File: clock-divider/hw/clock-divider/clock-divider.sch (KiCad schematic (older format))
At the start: 15 parts

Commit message: clock-divider: schematic++
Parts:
- added C? (x2): 22p, symbol Device:C
- added D?: Beat, symbol Device:LED
- added J?: AVR-ISP-6, symbol Connector:AVR-ISP-6
- added J?: Trigger Next Seq, symbol Connector:AudioJack3
- added Q? (x2): BC548, Package_TO_SOT_THT:TO-92_Inline, symbol Transistor_BJT:BC548
- added R? (x3): 3.3k, symbol Device:R
- added R?: R, symbol Device:R
- added R? (x9): 150, symbol Device:R
- added R? (x2): 10k, symbol Device:R
- added RV?: VAL_IN, symbol Device:R_POT
- added RV?: VAL_OUT, symbol Device:R_POT
- added SW?: Mode_in, symbol Switch:SW_Push
- added SW?: Mode_out, symbol Switch:SW_Push
- added SW?: Disp_next_seq, symbol Switch:SW_Push
- added U?: Left, Display_7Segment:HDSP-7801, symbol Display_Character:HDSP-7803
- added U?: Right, Display_7Segment:HDSP-7801, symbol Display_Character:HDSP-7803
- added Y?: 10MHz, symbol Device:Crystal
- C? (x2): value CP -> 100µ
- D? (x3): value D -> 1N4148
- R?: value R -> 10k
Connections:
- net labels added: +5V, 7seg_a, 7seg_b, 7seg_c, 7seg_d, 7seg_dp, 7seg_e, 7seg_f, 7seg_g, 7seg_sel_left, 7seg_sel_right, act_in, act_out, disp_next_seq, miso, mosi, sck, trig_next_seq, value_in, value_out, ~reset
- wire segments 38 -> 86
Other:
- moved on the sheet: R?, U?

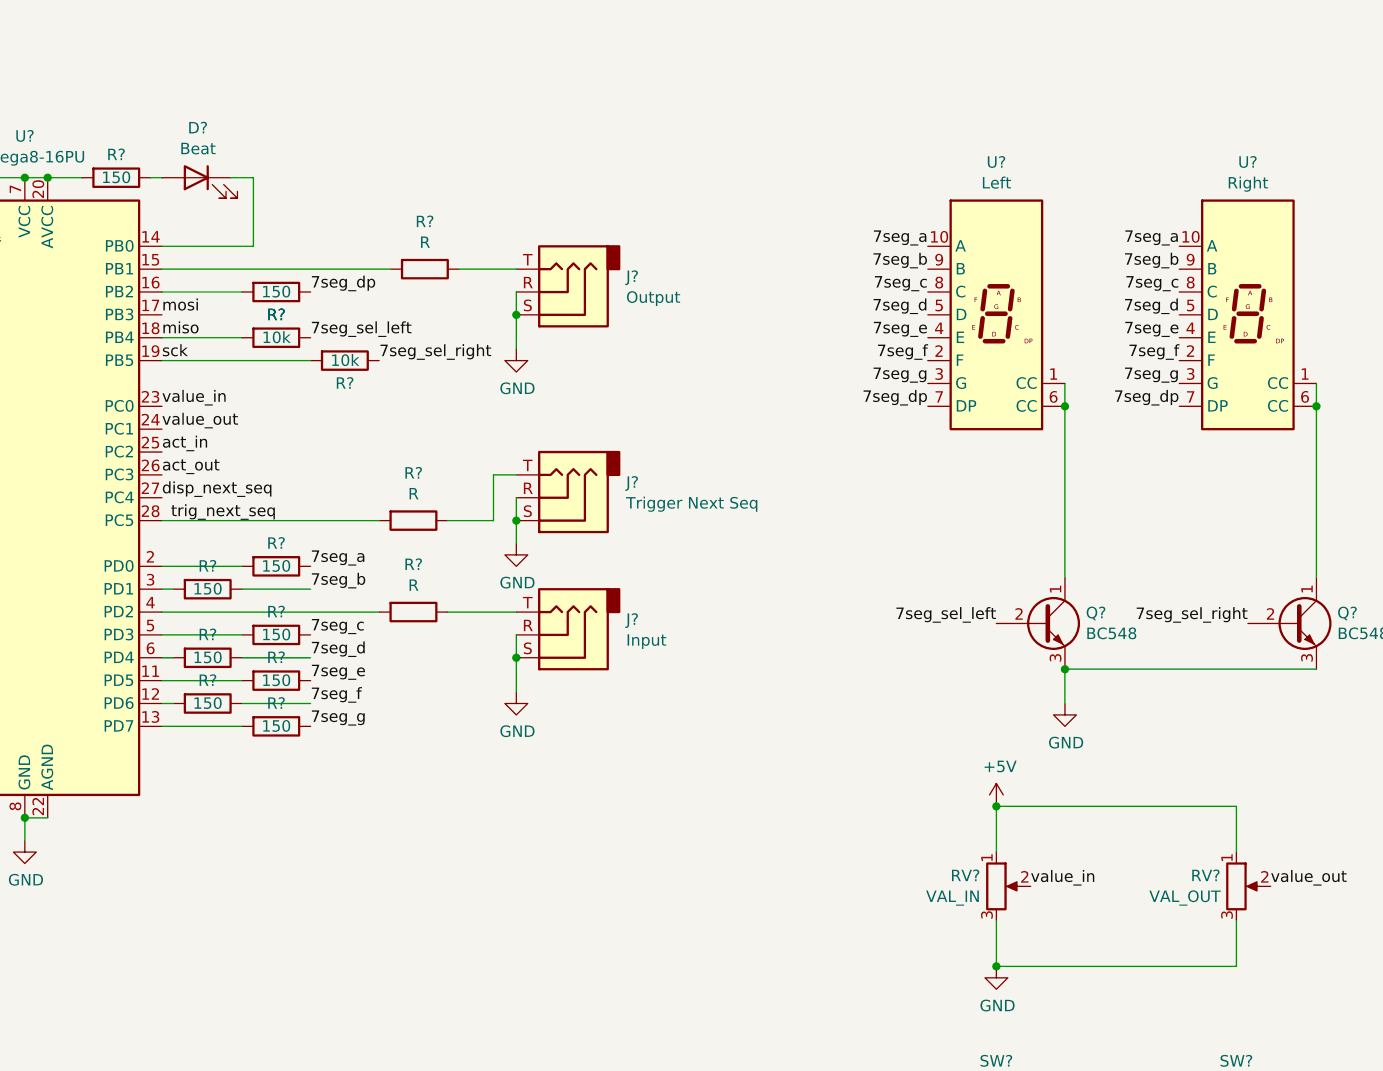
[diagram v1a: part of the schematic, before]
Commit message: clock-divider: add protection diodes
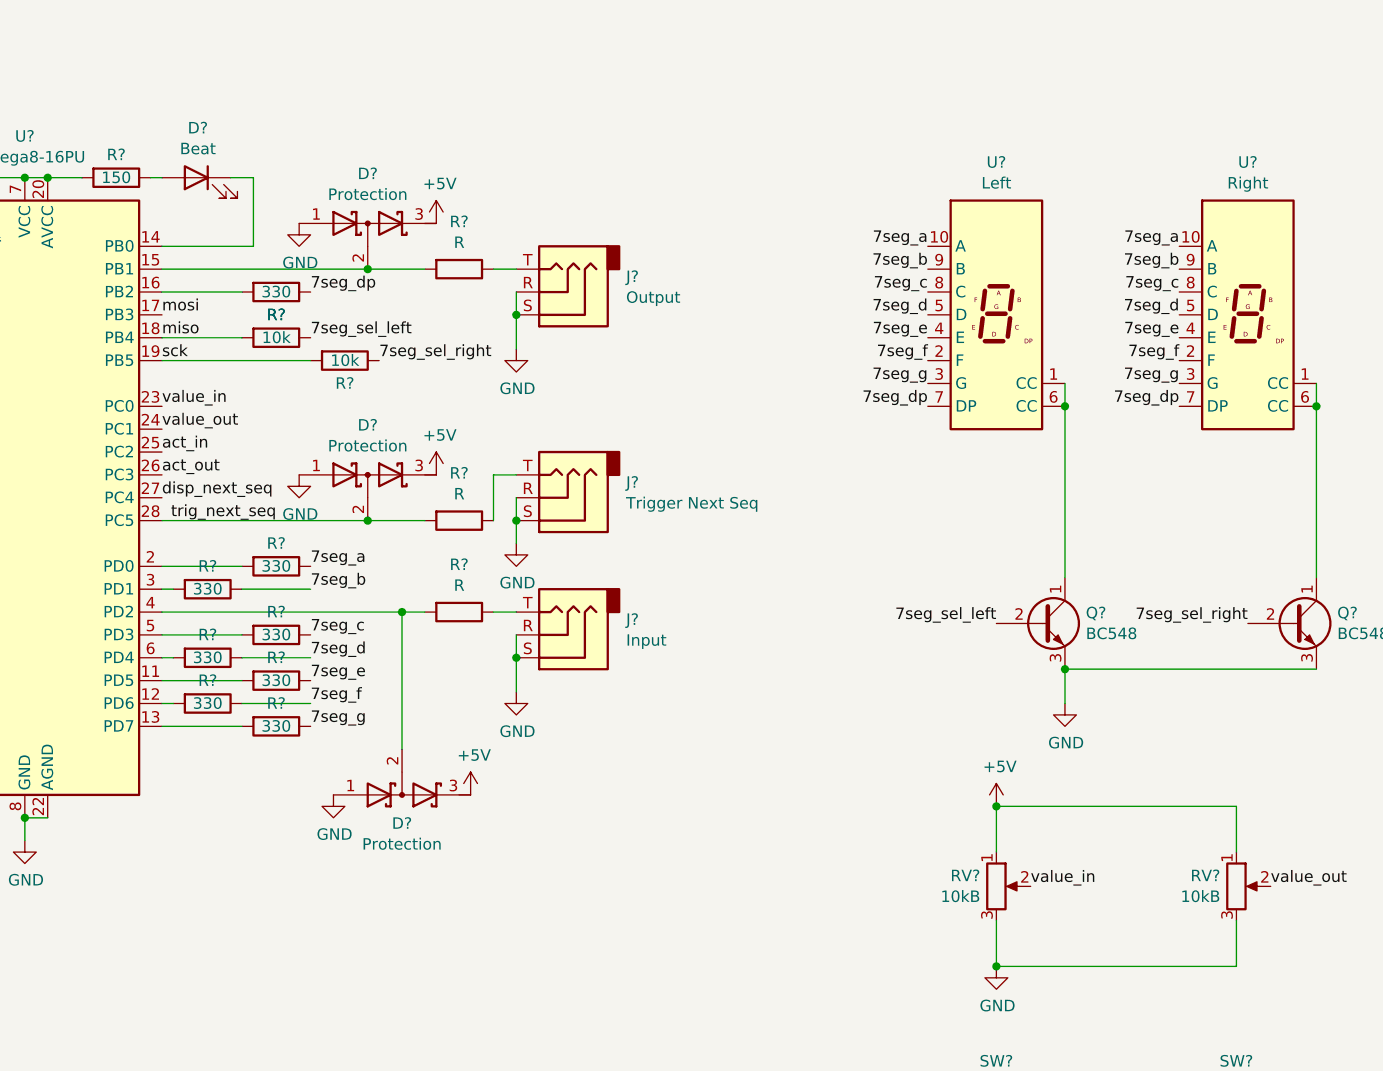
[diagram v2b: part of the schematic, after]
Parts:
- added D? (x3): Protection, symbol Device:D_Schottky_x2_Serial_ACK
- R? (x8): value 150 -> 330
- RV?: value VAL_IN -> 10kB
- RV?: value VAL_OUT -> 10kB
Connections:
- wire segments 86 -> 89
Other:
- moved on the sheet: R?
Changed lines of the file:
@@
 L Device:R R?
 U 1 1 60565DEB
-P 6050 1900
-F 0 "R?" V 5843 1900 50  0000 C CNN
-F 1 "R" V 5934 1900 50  0000 C CNN
-F 2 "" V 5980 1900 50  0001 C CNN
-F 3 "~" H 6050 1900 50  0001 C CNN
-	1    6050 1900
-	0    1    1    0
-$EndComp
-Wire Wire Line
-	6200 1900 6450 1900
-Wire Wire Line
-	5900 1900 4900 1900
+P 6200 1900
+F 0 "R?" V 5993 1900 50  0000 C CNN
+F 1 "R" V 6084 1900 50  0000 C CNN
+F 2 "" V 6130 1900 50  0001 C CNN
+F 3 "~" H 6200 1900 50  0001 C CNN
+	1    6200 1900
+	0    1    1    0
+$EndComp
+Wire Wire Line
+	6350 1900 6450 1900
+Wire Wire Line
+	6050 1900 5800 1900
 $Comp
 L power:GND #PWR?
@@
 L Device:R R?
 U 1 1 605A55C4
-P 6000 3400
-F 0 "R?" V 5793 3400 50  0000 C CNN
-F 1 "R" V 5884 3400 50  0000 C CNN
-F 2 "" V 5930 3400 50  0001 C CNN
-F 3 "~" H 6000 3400 50  0001 C CNN
-	1    6000 3400
-	0    1    1    0
-$EndComp
-Wire Wire Line
-	5850 3400 4900 3400
-Wire Wire Line
-	6450 3400 6150 3400
+P 6200 3400
+F 0 "R?" V 5993 3400 50  0000 C CNN
+F 1 "R" V 6084 3400 50  0000 C CNN
+F 2 "" V 6130 3400 50  0001 C CNN
+F 3 "~" H 6200 3400 50  0001 C CNN
+	1    6200 3400
+	0    1    1    0
+$EndComp
+Wire Wire Line
+	6050 3400 5950 3400
+Wire Wire Line
+	6450 3400 6350 3400
 $Comp
 L power:GND #PWR?
@@
 P 8550 4600
 F 0 "RV?" H 8480 4646 50  0000 R CNN
-F 1 "VAL_IN" H 8480 4555 50  0000 R CNN
+F 1 "10kB" H 8480 4555 50  0000 R CNN
 F 2 "" H 8550 4600 50  0001 C CNN
 F 3 "~" H 8550 4600 50  0001 C CNN
@@
 U 1 1 60631CFB
 P 9600 4600
-F 0 "RV?" H 9531 4646 50  0000 R CNN
-F 1 "VAL_OUT" H 9531 4555 50  0000 R CNN
+F 0 "RV?" H 9530 4646 50  0000 R CNN
+F 1 "10kB" H 9530 4555 50  0000 R CNN
 F 2 "" H 9600 4600 50  0001 C CNN
 F 3 "~" H 9600 4600 50  0001 C CNN
@@
 L Device:R R?
 U 1 1 607538BE
-P 6000 3000
-F 0 "R?" V 5793 3000 50  0000 C CNN
-F 1 "R" V 5884 3000 50  0000 C CNN
-F 2 "" V 5930 3000 50  0001 C CNN
-F 3 "~" H 6000 3000 50  0001 C CNN
-	1    6000 3000
-	0    1    1    0
-$EndComp
-Wire Wire Line
-	5850 3000 4900 3000
-Wire Wire Line
-	6150 3000 6350 3000
+P 6200 3000
+F 0 "R?" V 5993 3000 50  0000 C CNN
+F 1 "R" V 6084 3000 50  0000 C CNN
+F 2 "" V 6130 3000 50  0001 C CNN
+F 3 "~" H 6200 3000 50  0001 C CNN
+	1    6200 3000
+	0    1    1    0
+$EndComp
+Wire Wire Line
+	6050 3000 5800 3000
 Wire Wire Line
 	6350 3000 6350 2800
@@
 P 5400 3200
 F 0 "R?" V 5300 3200 50  0000 C CNN
-F 1 "150" V 5400 3200 50  0000 C CNN
+F 1 "330" V 5400 3200 50  0000 C CNN
 F 2 "" V 5330 3200 50  0001 C CNN
 F 3 "~" H 5400 3200 50  0001 C CNN
@@
 P 5100 3300
 F 0 "R?" V 5000 3300 50  0000 C CNN
-F 1 "150" V 5100 3300 50  0000 C CNN
+F 1 "330" V 5100 3300 50  0000 C CNN
 F 2 "" V 5030 3300 50  0001 C CNN
 F 3 "~" H 5100 3300 50  0001 C CNN
@@
 P 5400 3500
 F 0 "R?" V 5300 3500 50  0000 C CNN
-F 1 "150" V 5400 3500 50  0000 C CNN
+F 1 "330" V 5400 3500 50  0000 C CNN
 F 2 "" V 5330 3500 50  0001 C CNN
 F 3 "~" H 5400 3500 50  0001 C CNN
@@
 P 5100 3600
 F 0 "R?" V 5000 3600 50  0000 C CNN
-F 1 "150" V 5100 3600 50  0000 C CNN
+F 1 "330" V 5100 3600 50  0000 C CNN
 F 2 "" V 5030 3600 50  0001 C CNN
 F 3 "~" H 5100 3600 50  0001 C CNN
@@
 P 5400 3700
 F 0 "R?" V 5300 3700 50  0000 C CNN
-F 1 "150" V 5400 3700 50  0000 C CNN
+F 1 "330" V 5400 3700 50  0000 C CNN
 F 2 "" V 5330 3700 50  0001 C CNN
 F 3 "~" H 5400 3700 50  0001 C CNN
@@
 P 5100 3800
 F 0 "R?" V 5000 3800 50  0000 C CNN
-F 1 "150" V 5100 3800 50  0000 C CNN
+F 1 "330" V 5100 3800 50  0000 C CNN
 F 2 "" V 5030 3800 50  0001 C CNN
 F 3 "~" H 5100 3800 50  0001 C CNN
@@
 P 5400 3900
 F 0 "R?" V 5300 3900 50  0000 C CNN
-F 1 "150" V 5400 3900 50  0000 C CNN
+F 1 "330" V 5400 3900 50  0000 C CNN
 F 2 "" V 5330 3900 50  0001 C CNN
 F 3 "~" H 5400 3900 50  0001 C CNN
@@
 P 5400 2000
 F 0 "R?" V 5500 2000 50  0000 C CNN
-F 1 "150" V 5400 2000 50  0000 C CNN
+F 1 "330" V 5400 2000 50  0000 C CNN
 F 2 "" V 5330 2000 50  0001 C CNN
 F 3 "~" H 5400 2000 50  0001 C CNN
@@
 Wire Wire Line
 	3600 1500 4300 1500
+$Comp
+L Device:D_Schottky_x2_Serial_ACK D?
+U 1 1 608A614B
+P 5800 1700
+F 0 "D?" H 5800 1917 50  0000 C CNN
+F 1 "Protection" H 5800 1826 50  0000 C CNN
+F 2 "" H 5800 1700 50  0001 C CNN
+F 3 "~" H 5800 1700 50  0001 C CNN
+	1    5800 1700
+	1    0    0    -1
+$EndComp
+Connection ~ 5800 1900
+Wire Wire Line
+	5800 1900 4900 1900
+$Comp
+L power:GND #PWR?
+U 1 1 608A8846
+P 5500 1700
+F 0 "#PWR?" H 5500 1450 50  0001 C CNN
+F 1 "GND" H 5505 1527 50  0000 C CNN
+F 2 "" H 5500 1700 50  0001 C CNN
+F 3 "" H 5500 1700 50  0001 C CNN
+	1    5500 1700
+	1    0    0    -1
+$EndComp
+$Comp
+L power:+5V #PWR?
+U 1 1 608A92C9
+P 6100 1700
+F 0 "#PWR?" H 6100 1550 50  0001 C CNN
+F 1 "+5V" H 6115 1873 50  0000 C CNN
+F 2 "" H 6100 1700 50  0001 C CNN
+F 3 "" H 6100 1700 50  0001 C CNN
+	1    6100 1700
+	1    0    0    -1
+$EndComp
+$Comp
+L Device:D_Schottky_x2_Serial_ACK D?
+U 1 1 608AAF4E
+P 5800 2800
+F 0 "D?" H 5800 3017 50  0000 C CNN
+F 1 "Protection" H 5800 2926 50  0000 C CNN
+F 2 "" H 5800 2800 50  0001 C CNN
+F 3 "~" H 5800 2800 50  0001 C CNN
+	1    5800 2800
+	1    0    0    -1
+$EndComp
+$Comp
+L power:+5V #PWR?
+U 1 1 608AC722
+P 6100 2800
+F 0 "#PWR?" H 6100 2650 50  0001 C CNN
+F 1 "+5V" H 6115 2973 50  0000 C CNN
+F 2 "" H 6100 2800 50  0001 C CNN
+F 3 "" H 6100 2800 50  0001 C CNN
+	1    6100 2800
+	1    0    0    -1
+$EndComp
+Connection ~ 5800 3000
+Wire Wire Line
+	4900 3000 5800 3000
+$Comp
+L power:GND #PWR?
+U 1 1 608B8A53
+P 5500 2800
+F 0 "#PWR?" H 5500 2550 50  0001 C CNN
+F 1 "GND" H 5505 2627 50  0000 C CNN
+F 2 "" H 5500 2800 50  0001 C CNN
+F 3 "" H 5500 2800 50  0001 C CNN
+	1    5500 2800
+	1    0    0    -1
+$EndComp
+$Comp
+L Device:D_Schottky_x2_Serial_ACK D?
+U 1 1 608BB181
+P 5950 4200
+F 0 "D?" H 5950 4325 50  0000 C CNN
+F 1 "Protection" H 5950 4416 50  0000 C CNN
+F 2 "" H 5950 4200 50  0001 C CNN
+F 3 "~" H 5950 4200 50  0001 C CNN
+	1    5950 4200
+	1    0    0    1
+$EndComp
+Wire Wire Line
+	5950 4000 5950 3400
+Connection ~ 5950 3400
+Wire Wire Line
+	5950 3400 4900 3400
+$Comp
+L power:GND #PWR?
+U 1 1 608C0F8A
+P 5650 4200
+F 0 "#PWR?" H 5650 3950 50  0001 C CNN
+F 1 "GND" H 5655 4027 50  0000 C CNN
+F 2 "" H 5650 4200 50  0001 C CNN
+F 3 "" H 5650 4200 50  0001 C CNN
+	1    5650 4200
+	1    0    0    -1
+$EndComp
+$Comp
+L power:+5V #PWR?
+U 1 1 608C18E5
+P 6250 4200
+F 0 "#PWR?" H 6250 4050 50  0001 C CNN
+F 1 "+5V" H 6265 4373 50  0000 C CNN
+F 2 "" H 6250 4200 50  0001 C CNN
+F 3 "" H 6250 4200 50  0001 C CNN
+	1    6250 4200
+	1    0    0    -1
+$EndComp
 $EndSCHEMATC

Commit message: clock-divider: set values of input/output resistors to 10k
The value was experimentally determined by connecting a Beatstep Pro and
a PO-32.
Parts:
- R? (x3): value R -> 10k
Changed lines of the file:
@@
 P 6200 1900
 F 0 "R?" V 5993 1900 50  0000 C CNN
-F 1 "R" V 6084 1900 50  0000 C CNN
+F 1 "10k" V 6084 1900 50  0000 C CNN
 F 2 "" V 6130 1900 50  0001 C CNN
 F 3 "~" H 6200 1900 50  0001 C CNN
@@
 P 6200 3400
 F 0 "R?" V 5993 3400 50  0000 C CNN
-F 1 "R" V 6084 3400 50  0000 C CNN
+F 1 "10k" V 6084 3400 50  0000 C CNN
 F 2 "" V 6130 3400 50  0001 C CNN
 F 3 "~" H 6200 3400 50  0001 C CNN
@@
 P 6200 3000
 F 0 "R?" V 5993 3000 50  0000 C CNN
-F 1 "R" V 6084 3000 50  0000 C CNN
+F 1 "10k" V 6084 3000 50  0000 C CNN
 F 2 "" V 6130 3000 50  0001 C CNN
 F 3 "~" H 6200 3000 50  0001 C CNN

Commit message: clock-divider: hw cleanup
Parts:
- removed J?: Jack-DC, symbol Connector:Jack-DC
- removed U?: L78L05_SO8, Package_SO:SOIC-8_3.9x4.9mm_P1.27mm, symbol Regulator_Linear:L78L05_SO8
- added J?: Barrel_Jack_Switch, symbol Connector:Barrel_Jack_Switch
- added U?: L78L05_TO92, Package_TO_SOT_THT:TO-92_Inline, symbol Regulator_Linear:L78L05_TO92
- J?: value USB_B -> USB power
- J?: value AVR-ISP-6 -> ISP
- R?: value 150 -> 330
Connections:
- no-connect marks 0 -> 3
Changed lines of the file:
@@
 	6450 2100 6450 2000
-$Comp
-L Regulator_Linear:L78L05_SO8 U?
-U 1 1 6056B8C9
-P 1950 1950
-F 0 "U?" H 1950 2192 50  0000 C CNN
-F 1 "L78L05_SO8" H 1950 2101 50  0000 C CNN
-F 2 "Package_SO:SOIC-8_3.9x4.9mm_P1.27mm" H 2050 2150 50  0001 C CIN
-F 3 "http://www.st.com/content/ccc/resource/technical/document/datasheet/15/55/e5/aa/23/5b/43/fd/CD00000446.pdf/files/CD00000446.pdf/jcr:content/translations/en.CD00000446.pdf" H 2150 1950 50  0001 C CNN
-	1    1950 1950
-	1    0    0    -1
-$EndComp
 $Comp
 L Device:D D?
@@
 $EndComp
 $Comp
-L Connector:Jack-DC J?
-U 1 1 6056F0AD
-P 850 2050
-F 0 "J?" H 907 2375 50  0000 C CNN
-F 1 "Jack-DC" H 907 2284 50  0000 C CNN
-F 2 "" H 900 2010 50  0001 C CNN
-F 3 "~" H 900 2010 50  0001 C CNN
-	1    850  2050
-	1    0    0    -1
-$EndComp
-$Comp
 L Device:CP C?
 U 1 1 6056FBD8
@@
 P 850 1100
 F 0 "J?" H 907 1567 50  0000 C CNN
-F 1 "USB_B" H 907 1476 50  0000 C CNN
+F 1 "USB power" H 907 1476 50  0000 C CNN
 F 2 "" H 1000 1050 50  0001 C CNN
 F 3 " ~" H 1000 1050 50  0001 C CNN
@@
 P 1600 3650
 F 0 "J?" H 1271 3746 50  0000 R CNN
-F 1 "AVR-ISP-6" H 1271 3655 50  0000 R CNN
+F 1 "ISP" H 1271 3655 50  0000 R CNN
 F 2 "" V 1350 3700 50  0001 C CNN
 F 3 " ~" H 325 3100 50  0001 C CNN
@@
 P 4700 1500
 F 0 "R?" V 4600 1500 50  0000 C CNN
-F 1 "150" V 4700 1500 50  0000 C CNN
+F 1 "330" V 4700 1500 50  0000 C CNN
 F 2 "" V 4630 1500 50  0001 C CNN
 F 3 "~" H 4700 1500 50  0001 C CNN
@@
 	1    0    0    -1
 $EndComp
+$Comp
+L Regulator_Linear:L78L05_TO92 U?
+U 1 1 608E6899
+P 1950 1950
+F 0 "U?" H 1950 2192 50  0000 C CNN
+F 1 "L78L05_TO92" H 1950 2101 50  0000 C CNN
+F 2 "Package_TO_SOT_THT:TO-92_Inline" H 1950 2175 50  0001 C CIN
+F 3 "http://www.st.com/content/ccc/resource/technical/document/datasheet/15/55/e5/aa/23/5b/43/fd/CD00000446.pdf/files/CD00000446.pdf/jcr:content/translations/en.CD00000446.pdf" H 1950 1900 50  0001 C CNN
+	1    1950 1950
+	1    0    0    -1
+$EndComp
+$Comp
+L Connector:Barrel_Jack_Switch J?
+U 1 1 608F218A
+P 850 2050
+F 0 "J?" H 907 2367 50  0000 C CNN
+F 1 "Barrel_Jack_Switch" H 907 2276 50  0000 C CNN
+F 2 "" H 900 2010 50  0001 C CNN
+F 3 "~" H 900 2010 50  0001 C CNN
+	1    850  2050
+	1    0    0    -1
+$EndComp
+NoConn ~ 1150 2050
+NoConn ~ 1150 1100
+NoConn ~ 1150 1200
 $EndSCHEMATC
